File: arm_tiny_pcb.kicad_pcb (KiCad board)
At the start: 2 copper layers, 26 x 36 mm, 26 parts, among them J1 Conn_01x09_Pin, J2 Conn_01x09_Pin, J3 Conn_02x02_Top_Bottom, SW1 SKRKAEE020, SW2 SKRKAEE020, U1 STM32F042F6P6, U2 XBL1117-3.3/STR, U3 USBLC6-2SC6

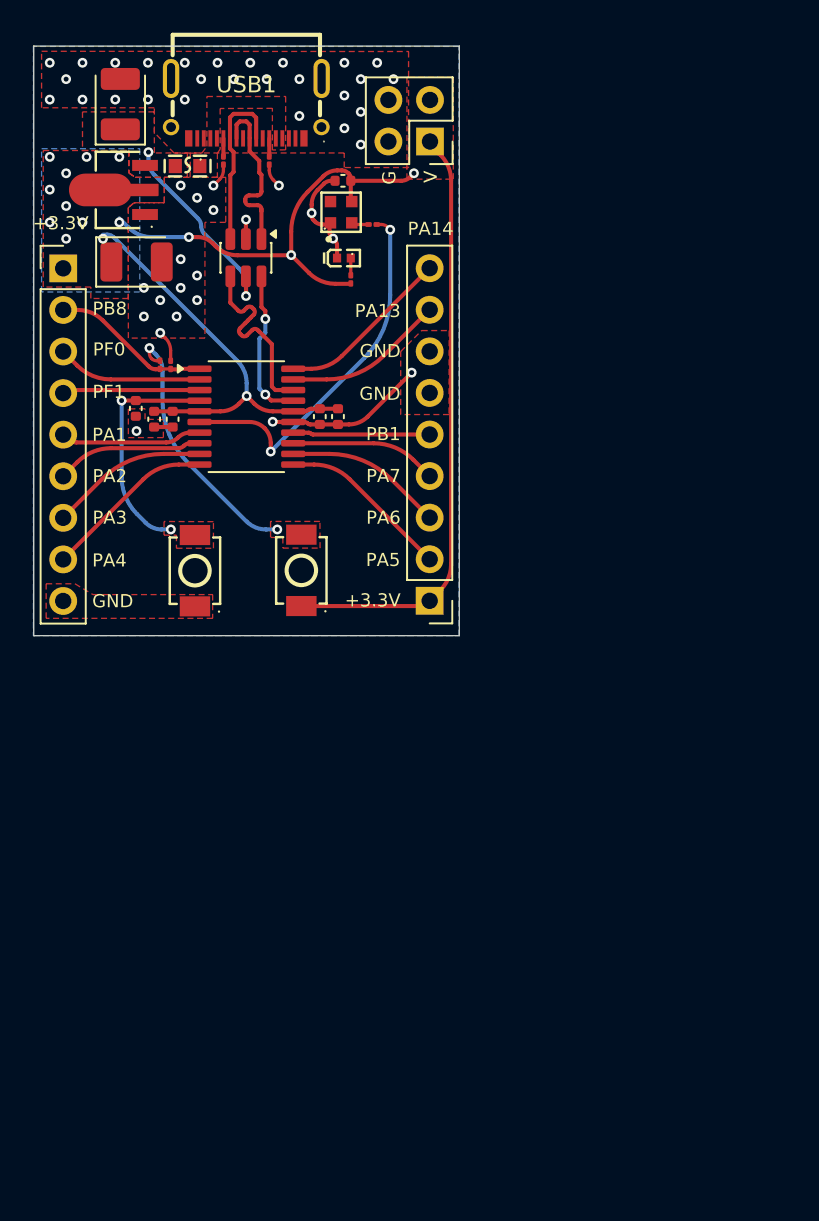
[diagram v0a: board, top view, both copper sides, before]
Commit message: Hardware Rev 2: 20x38.5mm, TVS protection, ME6211 LDO & portable libs
Major hardware revision, project library centralization, and documentation overhaul:

1. Hardware & PCB:
- Updated board dimensions to 20 mm × 38.5 mm (compact, breadboard-friendly layout).
- Added SD05-01FTG TVS diode (SOD-323) on VBUS for ESD and transient surge protection.
- Replaced LDO regulator with low-noise, low-Iq ME6211C33M5G-N (SOT-23-5).
- Replaced tantalum capacitors with MLCC X7R 0805 ceramic capacitors (C1 2.2 µF & C2 1 µF).
- Updated resistor footprints to standard 0402 package (R_0402_1005Metric).
- Optimized power routing, ground stitching vias, and bottom GND return planes.

2. KiCad Libraries & Portability:
- Consolidated project symbols, footprints, and 3D models into self-contained NanoCortex libraries.
- Bundled .wrl 3D models using project-relative paths (${KIPRJMOD}) for seamless multi-machine compatibility.
- Cleaned up obsolete legacy libraries (libs_footprints, libs_symbols).
- Added project library tables (sym-lib-table and fp-lib-table).
- Added .gitignore to exclude KiCad local history, caches, and .lck lock files.

3. Documentation & Media:
- Generated high-quality raytraced 3D renders (top view & isometric perspective).
- Exported vector schematic PDF (arm_tiny_pcb_sch.pdf) and embedded preview graphic.
- Completely overhauled README.md and README_FR.md with full pinout tables, specs, and BOM.
- Expanded roadmap into 3 concrete embedded application tracks: drone telemetry subsystem, hybrid USB-MIDI / op-amp synth, and 40W+ USB-PD Buck converter lab.
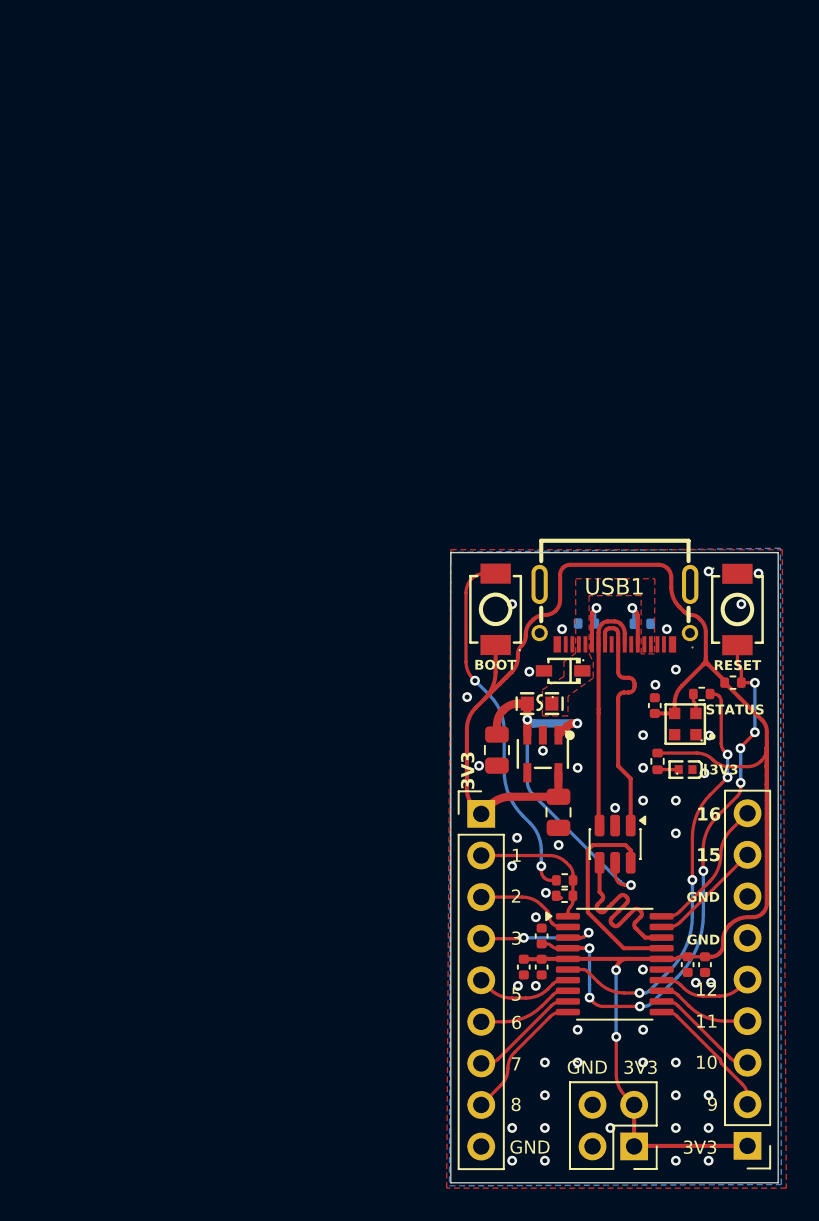
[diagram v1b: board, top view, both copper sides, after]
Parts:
- removed U2: XBL1117-3.3/STR, easyeda2kicad:SOT-89-3_L4.5-W2.4-P1.50-LS4.0-BR
- added D1: SD05-01FTG, NanoCortex:SOD-323_L1.8-W1.3-LS2.5-RD, F.Cu at (156.4, 71.2)
- added LDO1: ME6211C33M5G-N, NanoCortex:SOT-23-5_L3.0-W1.7-P0.95-LS2.8-BL, F.Cu at (155.1, 76.2)
- added R7: 10k, Resistor_SMD:R_0402_1005Metric, F.Cu at (166.7, 71.9)
- C1: value 10u -> 2.2u / 25V / X7R; footprint Capacitor_Tantalum_SMD:CP_EIA-3528-21_Kemet-B -> Capacitor_SMD:C_0805_2012Metric
- C2: value 22u -> 1u / 25V / X7R; footprint Capacitor_Tantalum_SMD:CP_EIA-3528-21_Kemet-B -> Capacitor_SMD:C_0805_2012Metric
- F1: footprint easyeda2kicad:F0603 -> NanoCortex:F0603
- LED1: footprint easyeda2kicad:LED0402-R-RD -> NanoCortex:LED0402-R-RD
- LED2: footprint easyeda2kicad:LED-SMD_4P-L2.0-W2.0-TL_J-ST2020RGB-IC-P4-5-SO1 -> NanoCortex:LED-SMD_4P-L2.0-W2.0-TL_J-ST2020RGB-IC-P4-5-SO1
- R1, R2: footprint Resistor_SMD:R_01005_0402Metric -> Resistor_SMD:R_0402_1005Metric; moved to B.Cu
- R3, R4, R5, R6: footprint Resistor_SMD:R_01005_0402Metric -> Resistor_SMD:R_0402_1005Metric
- SW1, SW2: footprint easyeda2kicad:SW-SMD_L3.9-W3.0-P4.45 -> NanoCortex:SW-SMD_L3.9-W3.0-P4.45
- USB1: footprint easyeda2kicad:TYPE-C-SMD_GT-USB-7025 -> NanoCortex:TYPE-C-SMD_GT-USB-7025
- moved J3 62.6 mm to (160.7, 100.2)
- moved C1 50.9 mm to (156.1, 79.8), turned to -90 degrees
- moved U3 42.3 mm to (159.5, 81.7)
- moved J1 42.0 mm to (151.4, 79.9)
- moved C7 40.7 mm to (155.1, 87.3), turned to 90 degrees
- moved R4 40.4 mm to (156.4, 84.9), turned to 0 degrees
- moved C6 40.4 mm to (154.0, 89.2)
- moved C5 40.4 mm to (155.1, 89.2)
- moved C3 40.3 mm to (164.0, 89.1)
- moved U1 40.3 mm to (159.5, 89.1)
- moved C4 40.3 mm to (165.0, 89.1)
- moved R3 40.0 mm to (156.5, 84.0), turned to 0 degrees
- moved F1 39.3 mm to (154.9, 73.2)
- moved J2 38.5 mm to (167.6, 100.2)
- moved USB1 38.2 mm to (159.5, 67.7)
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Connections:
- C1 pad 1: +5V -> +3.3V
- C2 pad 1: +3.3V -> +5V
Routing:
- net GND: track 24.2 -> 0.24 mm, vias 47 -> 49
- net NRST: track 14.4 -> 35.0 mm, vias 2 -> 8
- net +3.3V: track 91.1 -> 107.0 mm, vias 15 -> 2
- net +5V: track 12.3 -> 24.6 mm, vias 2 -> 3
- net BOOT: track 15.9 -> 22.1 mm
- net D1-: track 10.6 -> 15.3 mm
- net D1+: track 10.6 -> 15.0 mm
- net D-: track 9.68 -> 12.9 mm, vias 2 -> 0
- net GPIO11: track 9.00 -> 5.82 mm
- net GPIO6: track 8.97 -> 5.89 mm
- net GPIO10: track 9.69 -> 6.71 mm
- net LED_STATUS: track 22.8 -> 25.8 mm, vias 2 -> 4
- net GPIO7: track 9.69 -> 6.78 mm
- net GPIO15: track 9.86 -> 7.03 mm
- net GPIO2: track 8.89 -> 6.15 mm
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- removed copper zone on B.Cu, net +3.3V
- removed copper zone on F.Cu, net +3.3V
- removed copper zone on F.Cu, net +5V
- removed copper zone on F.Cu, net BOOT
- removed copper zone on F.Cu, net NRST
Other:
- board size 26 x 36 mm -> 20 x 38.5 mm
- board text added: "1"
- board text added: "10"
- board text added: "11"
- board text added: "12"
- board text added: "15"
- board text added: "16"
- board text added: "2"
- board text added: "3"
- board text added: "3V3"
- board text added: "5"
- board text added: "6"
- board text added: "7"
- board text added: "8"
- board text added: "9"
- board text added: "BOOT"
- board text added: "RESET"
- board text removed: "+3.3V"
- board text removed: "G"
- board text removed: "PA1"
- board text removed: "PA13"
- board text removed: "PA14"
- board text removed: "PA2"
- board text removed: "PA3"
- board text removed: "PA4"
- board text removed: "PA5"
- board text removed: "PA6"
- board text removed: "PA7"
- board text removed: "PB1"
- board text removed: "PB8"
- board text removed: "PF0"
- board text removed: "PF1"
- board text removed: "V"

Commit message: feat(hw): upgrade RGB LED to WS2812B-V6, expose 5V/NRST & introduce CaveRover branding
- Update on-board RGB status LED from SK6805 to WS2812B-2020-V6 for native 3.3V operation
- Add 100 nF decoupling capacitor (C8) adjacent to WS2812B VDD pin
- Update header pinout:
  * Expose protected 5V rail on J1 pin 1 (post-polyfuse F1) for drone receivers and external sensors
  * Expose dedicated hardware NRST on J2 pin 7 for ST-Link "Connect Under Reset" support
  * Complete standard 4-wire SWD debug header (GND, NRST, SWDIO, SWCLK)
- Introduce CaveRover project branding:
  * Add vertical "CAVEROVER" silkscreen text styled in Anurati futuristic font
  * Add custom 8-bit pixel art silkscreen logo footprint (Logo_CaveRover) to NanoCortex.pretty
  * Integrate CaveRover visual identity, badge, and logo into README.md & README_FR.md
- Fix technical inconsistencies in documentation:
  * Remove breadboard-friendly mentions
  * Highlight USART2 (PA2/PA3) as primary user serial port due to PA9/PA10 USB multiplexing
  * Clarify ADC allocation (ADC_IN0 dedicated to RGB LED, 7 external ADC channels available)
  * Add external pull-up warning on PB8 / BOOT0 pin
  * Remove unsupported CAN bus references from drone roadmap in favor of CRSF/SBUS UART
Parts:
- added LOGO**: Logo_CavityRover_F_SilkS, NanoCortex:Logo_CavityRover, B.Cu at (159.6, 75.3)
- LED2: value SK6805-EC20 -> WS2812B-2020-V6; footprint NanoCortex:LED-SMD_4P-L2.0-W2.0-TL_J-ST2020RGB-IC-P4-5-SO1 -> NanoCortex:LED-SMD_4P-L2.2-W2.0-P1.00_WS2815C-2020-4P
- moved F1 0.32 mm to (155.0, 72.8)
- moved C8 0.26 mm to (162.1, 73.1)
- turned LED2 to 90 degrees
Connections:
- J1 pad 1: +3.3V -> +5V
- J2 pad 7: GND -> NRST
- LED2 pad 1: GND -> unconnected-(LED2-DO-Pad1)
- LED2 pad 2: Net-(LED2-DIN) -> GND
- LED2 pad 3: +3.3V -> Net-(LED2-DI)
- LED2 pad 4: unconnected-(LED2-DOUT-Pad4) -> +3.3V
- R6 pad 2: Net-(LED2-DIN) -> Net-(LED2-DI)
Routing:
- net +5V: track 24.6 -> 29.9 mm, vias 3 -> 2
- net NRST: track 35.0 -> 38.1 mm
- net +3.3V: track 107.0 -> 105.3 mm, vias 2 -> 4
- net Net-(LED2-DI): track 0.00 -> 1.46 mm
- net Net-(LED2-DIN): track 1.24 -> 0.00 mm
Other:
- board text added: "5V"
- board text added: "CAVE ROVER"
- board text added: "NRST"
- board text added: "STATUS"
